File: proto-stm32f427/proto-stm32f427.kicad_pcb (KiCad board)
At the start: 2 copper layers, 54.6 x 66.7 mm, 37 parts, among them J1 Left, J2 Micro_SD_Card, J3 USB, J4 Debug, J5 Right, U1 NCV5501, U2 STM32F427VGTx, Y1 8 MHz

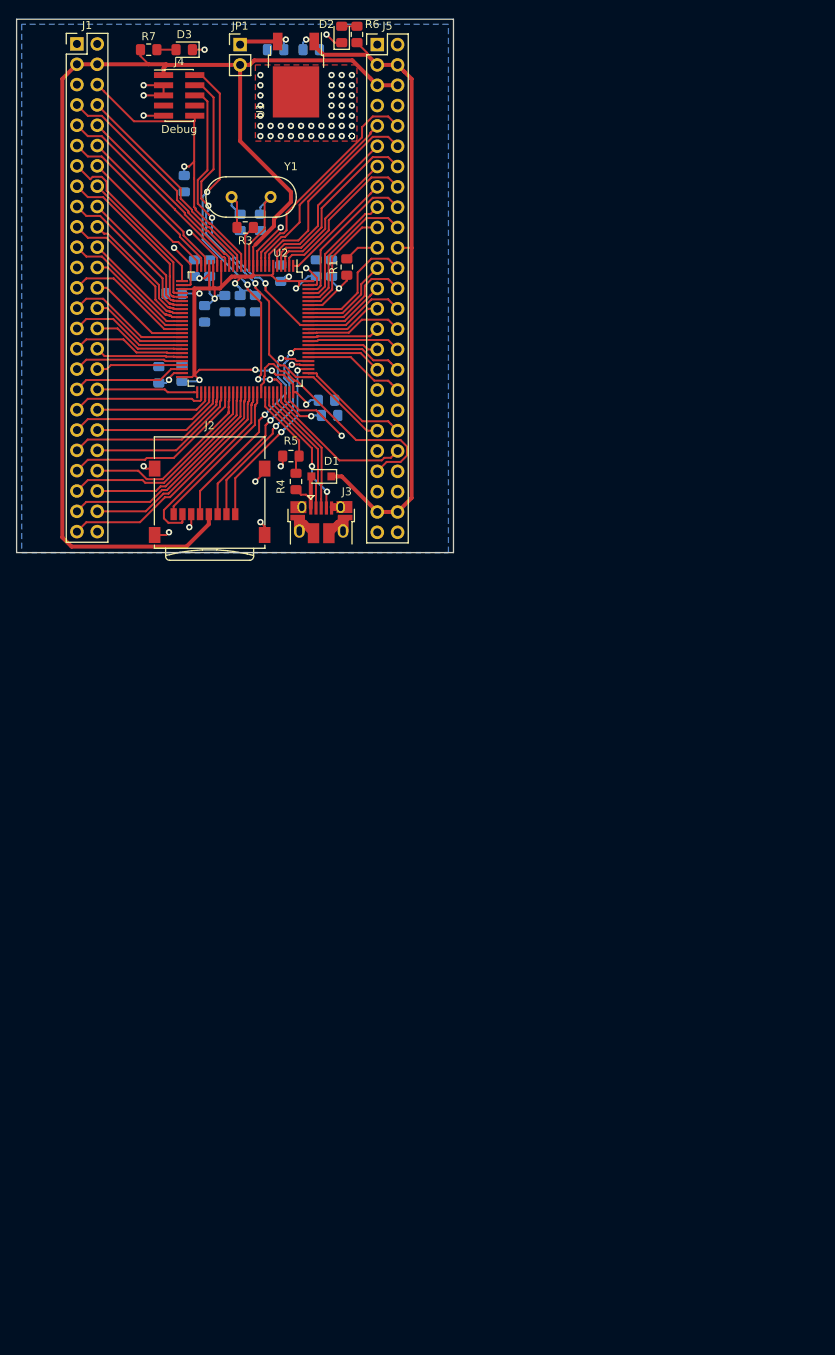
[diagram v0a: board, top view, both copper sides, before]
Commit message: New improved core board for stm32f427
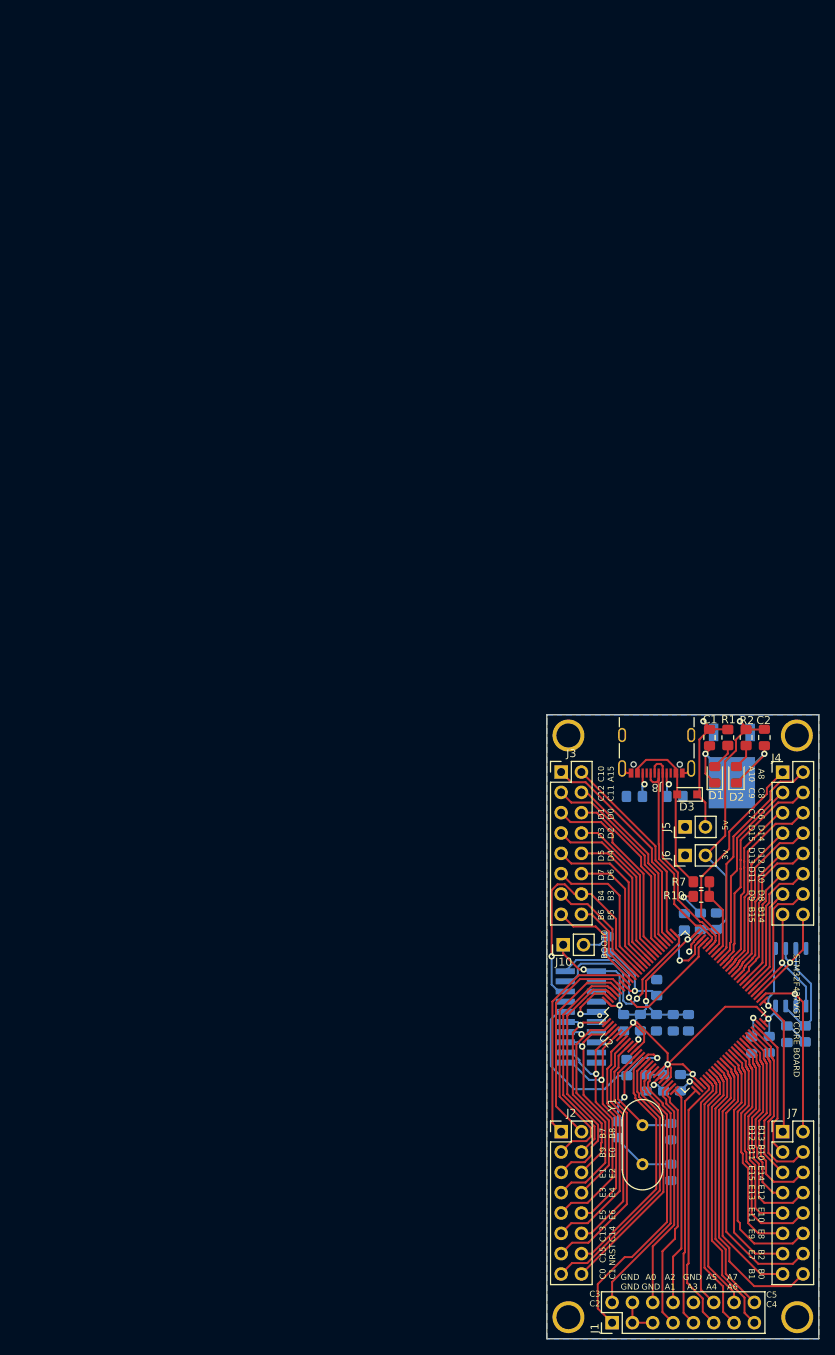
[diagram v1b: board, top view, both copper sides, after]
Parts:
- removed JP1: Idd, Connector_PinHeader_2.54mm:PinHeader_1x02_P2.54mm_Vertical
- added C19: 0.1 uF, Capacitor_SMD:C_0805_2012Metric_Pad1.18x1.45mm_HandSolder, B.Cu at (154.7, 147.8)
- added J10: BOOT, Connector_PinHeader_2.54mm:PinHeader_1x02_P2.54mm_Vertical, F.Cu at (126.7, 136.7)
- added J6: PWR_3v, Connector_PinHeader_2.54mm:PinHeader_1x02_P2.54mm_Vertical, F.Cu at (142.0, 125.5)
- added J7: Conn_02x08_Odd_Even, Connector_PinHeader_2.54mm:PinHeader_2x08_P2.54mm_Vertical, F.Cu at (154.2, 160.0)
- added J8: USB_C_Receptacle_USB2.0, Connector_USB:USB_C_Receptacle_GCT_USB4105-xx-A_16P_TopMnt_Horizontal, F.Cu at (138.4, 111.5)
- added J9: Conn_ARM_ETM_SWD_20, Connector_PinHeader_1.27mm:PinHeader_2x10_P1.27mm_Vertical_SMD, B.Cu at (128.9, 145.7)
- added R10: 10k, Resistor_SMD:R_0805_2012Metric_Pad1.20x1.40mm_HandSolder, F.Cu at (144.0, 130.6)
- added R8: 5.1k, Resistor_SMD:R_0805_2012Metric_Pad1.20x1.40mm_HandSolder, B.Cu at (140.7, 118.1)
- added R9: 10k, Resistor_SMD:R_0805_2012Metric_Pad1.20x1.40mm_HandSolder, B.Cu at (157.0, 147.8)
- added REF**: MountingHole_2.5mm_Pad, MountingHole:MountingHole_2.5mm_Pad, F.Cu at (156.0, 183.2)
- added REF**: MountingHole_2.5mm_Pad, MountingHole:MountingHole_2.5mm_Pad, F.Cu at (156.0, 110.5)
- added REF**: MountingHole_2.5mm_Pad, MountingHole:MountingHole_2.5mm_Pad, F.Cu at (127.4, 183.2)
- added REF**: MountingHole_2.5mm_Pad, MountingHole:MountingHole_2.5mm_Pad, F.Cu at (127.4, 110.5)
- added U3: W25Q32JVSS, Package_SO:SOIC-8_5.23x5.23mm_P1.27mm, B.Cu at (155.2, 140.7)
- C1, C2: moved to F.Cu
- C3, C5: value 16 pF -> 2.2 uF
- C4, C6: value 2.2 uF -> 16 pF
- D1: value BAT48JFILM -> LED; footprint Diode_SMD:D_SOD-323_HandSoldering -> LED_SMD:LED_0805_2012Metric_Pad1.15x1.40mm_HandSolder
- D3: value LED -> BAT48JFILM; footprint LED_SMD:LED_0805_2012Metric_Pad1.15x1.40mm_HandSolder -> Diode_SMD:D_SOD-323_HandSoldering
- J1: value Left -> Conn_02x08_Odd_Even; footprint Connector_PinHeader_2.54mm:PinHeader_2x25_P2.54mm_Vertical -> Connector_PinHeader_2.54mm:PinHeader_2x08_P2.54mm_Vertical
- J2: value Micro_SD_Card -> Conn_02x08_Odd_Even; footprint Connector_Card:microSD_HC_Wuerth_693072010801 -> Connector_PinHeader_2.54mm:PinHeader_2x08_P2.54mm_Vertical
- J3: value USB -> Conn_02x08_Odd_Even; footprint Connector_USB:USB_Micro-B_Amphenol_10103594-0001LF_Horizontal -> Connector_PinHeader_2.54mm:PinHeader_2x08_P2.54mm_Vertical
- J4: value Debug -> Conn_02x08_Odd_Even; footprint Connector_PinHeader_1.27mm:PinHeader_2x05_P1.27mm_Vertical_SMD -> Connector_PinHeader_2.54mm:PinHeader_2x08_P2.54mm_Vertical
- J5: value Right -> PWR_5v; footprint Connector_PinHeader_2.54mm:PinHeader_2x25_P2.54mm_Vertical -> Connector_PinHeader_2.54mm:PinHeader_1x02_P2.54mm_Vertical
- R1: value 1k -> 220; footprint Resistor_SMD:R_0805_2012Metric_Pad1.15x1.40mm_HandSolder -> Resistor_SMD:R_0805_2012Metric_Pad1.20x1.40mm_HandSolder
- R2: value 100k -> 220; footprint Resistor_SMD:R_0805_2012Metric_Pad1.15x1.40mm_HandSolder -> Resistor_SMD:R_0805_2012Metric_Pad1.20x1.40mm_HandSolder; moved to F.Cu
- R3: value 220 -> 1k; footprint Resistor_SMD:R_0805_2012Metric_Pad1.15x1.40mm_HandSolder -> Resistor_SMD:R_0805_2012Metric_Pad1.20x1.40mm_HandSolder; moved to B.Cu
- R4: value 4.7k -> 100k; footprint Resistor_SMD:R_0805_2012Metric_Pad1.15x1.40mm_HandSolder -> Resistor_SMD:R_0805_2012Metric_Pad1.20x1.40mm_HandSolder; moved to B.Cu
- R5: value 10k -> 220; footprint Resistor_SMD:R_0805_2012Metric_Pad1.15x1.40mm_HandSolder -> Resistor_SMD:R_0805_2012Metric_Pad1.20x1.40mm_HandSolder; moved to B.Cu
- R6: value 220 -> 5.1k; footprint Resistor_SMD:R_0805_2012Metric_Pad1.15x1.40mm_HandSolder -> Resistor_SMD:R_0805_2012Metric_Pad1.20x1.40mm_HandSolder; moved to B.Cu
- R7: value 220 -> 4.7k; footprint Resistor_SMD:R_0805_2012Metric_Pad1.15x1.40mm_HandSolder -> Resistor_SMD:R_0805_2012Metric_Pad1.20x1.40mm_HandSolder
- U1: moved to B.Cu
- moved J1 173.3 mm to (132.9, 183.9), turned to 90 degrees
- moved Y1 125.0 mm to (136.7, 159.2), turned to -90 degrees
- moved R7 124.9 mm to (144.0, 128.8), turned to 180 degrees
- moved C18 123.6 mm to (134.7, 152.0), turned to 90 degrees
- moved C17 120.8 mm to (152.5, 149.1), turned to 90 degrees
- moved C3 119.8 mm to (150.3, 149.2), turned to -90 degrees
- moved C7 115.5 mm to (137.1, 153.9), turned to -90 degrees
- moved C4 114.2 mm to (140.2, 160.0)
- moved J4 113.3 mm to (154.2, 115.1)
- moved C9 112.8 mm to (141.4, 153.9)
- moved D3 112.3 mm to (142.2, 117.9)
- moved C8 112.0 mm to (139.3, 153.9)
- moved C2 105.5 mm to (151.9, 110.7), turned to -90 degrees
- moved J5 105.1 mm to (142.0, 121.9), turned to 90 degrees
- moved C11 104.9 mm to (140.5, 146.4)
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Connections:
- C2 pad 1: /3v_regulated -> /3v_cpu
- C3 pad 1: GND -> Net-(C3-Pad1)
- C3 pad 2: /PH0 -> GND
- C4 pad 1: Net-(C4-Pad1) -> GND
- C4 pad 2: GND -> /PH0
- C5 pad 1: GND -> Net-(C5-Pad1)
- C5 pad 2: Net-(C5-Pad2) -> GND
- C6 pad 1: Net-(C6-Pad1) -> GND
- C6 pad 2: GND -> Net-(C6-Pad2)
- D1 pad 1: /5v -> GND
- D1 pad 2: /5v_usb -> Net-(D1-Pad2)
- D3 pad 1: GND -> /5v
- D3 pad 2: Net-(D3-Pad2) -> /5v_usb
- J1 pad 1: GND -> /PC2
- J1 pad 10: /PC2 -> GND
- J1 pad 11: /PA1 -> /PA4
- J1 pad 12: /PA0 -> /PA5
- J1 pad 13: /PA3 -> /PA6
- J1 pad 14: /PA2 -> /PA7
- J1 pad 15: /PA5 -> /PC4
- J1 pad 16: /PA4 -> /PC5
- J1 pad 2: GND -> /PC3
- J1 pad 3: /3v_cpu -> GND
- J1 pad 4: /3v_cpu -> GND
- J1 pad 6: /NRST -> /PA0
- J1 pad 7: /PC1 -> /PA1
- J1 pad 8: /PC0 -> /PA2
- J1 pad 9: /PC3 -> /PA3
- J2 pad 1: /PC10 -> /PB7
- J2 pad 2: /PC11 -> /PB8
- J2 pad 3: /PD2 -> /PB9
- J2 pad 4: /3v_cpu -> /PE0
- J2 pad 5: /PC12 -> /PE1
- J2 pad 6: GND -> /PE2
- J2 pad 7: /PC8 -> /PE3
- J2 pad 8: /PC9 -> /PE4
- J2 pad 9: GND -> /PE5
- J3 pad 1: /5v_usb -> /PC10
- J3 pad 2: /PA11 -> /PA15
- J3 pad 3: /PA12 -> /PC12
- J3 pad 4: /PA10 -> /PC11
- J3 pad 5: GND -> /PD1
- J3 pad 6: GND -> /PD0
- J4 pad 1: /3v_cpu -> /PA10
- J4 pad 10: /NRST -> /PD12
- J4 pad 2: /PA13 -> /PA8
- J4 pad 3: GND -> /PC9
- J4 pad 4: /PA14 -> /PC8
- J4 pad 5: GND -> /PC7
- J4 pad 6: /PB3 -> /PC6
- J4 pad 7: Net-(J4-Pad7) -> /PD15
- J4 pad 8: Net-(J4-Pad8) -> /PD14
- J4 pad 9: GND -> /PD13
- J5 pad 2: GND -> /5v
- R1 pad 1: Net-(R1-Pad1) -> /5v
- R1 pad 2: /BOOT0 -> Net-(D1-Pad2)
- R2 pad 1: GND -> /3v_cpu
- R2 pad 2: Net-(R1-Pad1) -> Net-(D2-Pad2)
- R3 pad 1: /PH1 -> Net-(R3-Pad1)
- R3 pad 2: Net-(C5-Pad2) -> /BOOT0
- R4 pad 1: /PA9 -> GND
- R4 pad 2: /5v_usb -> Net-(R3-Pad1)
- R5 pad 1: /PA9 -> /PH1
- R5 pad 2: GND -> Net-(C6-Pad2)
- R6 pad 1: /5v -> /CC2
- R6 pad 2: Net-(D2-Pad2) -> GND
- R7 pad 1: /3v_cpu -> /PA9
- R7 pad 2: Net-(D3-Pad2) -> /5v_usb
- U1 pad 3: /3v_regulated -> /3v_cpu
- U2 pad 49: Net-(C4-Pad1) -> Net-(C3-Pad1)
- U2 pad 73: Net-(C6-Pad1) -> Net-(C5-Pad1)
- U2 pad 94: Net-(R1-Pad1) -> Net-(R3-Pad1)
- Y1 pad 2: Net-(C5-Pad2) -> Net-(C6-Pad2)
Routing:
- net /3v_cpu: track 246.0 -> 138.5 mm, vias 10 -> 9
- net /5v: track 85.7 -> 18.8 mm
- net /PA13: track 67.4 -> 26.3 mm, vias 4 -> 1
- net /PA14: track 57.0 -> 25.5 mm, vias 2 -> 1
- net /PB0: track 14.2 -> 37.3 mm
- net /PB2: track 13.6 -> 34.5 mm
- net /PE8: track 12.4 -> 32.2 mm
- net /PD2: track 39.1 -> 20.0 mm, vias 2 -> 0
- net /NRST: track 38.0 -> 57.0 mm
- net /PC4: track 15.8 -> 34.7 mm
- net /PB3: track 50.0 -> 31.5 mm, vias 2 -> 1
- net /PE10: track 12.3 -> 29.6 mm
- net /PA6: track 16.9 -> 33.3 mm
- net /PE12: track 11.7 -> 27.2 mm
- net /PB1: track 17.0 -> 32.3 mm
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- removed copper zone on F.Cu, net GND
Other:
- board size 54.6 x 66.7 mm -> 34 x 78 mm
- net class Default removed
- board text added: "A0 GND"
- board text added: "A2 A1"
- board text added: "A5 A4"
- board text added: "A7 A6"
- board text added: "A8 A10"
- board text added: "B0 B1"
- board text added: "B10 B11"
- board text added: "B13 B12"
- board text added: "B14 B15"
- board text added: "B2 E7"
- board text added: "B4 B3"
- board text added: "B6 B5"
- board text added: "B7 B8"
- board text added: "B9 E0"
- board text added: "C0 C1"
- board text added: "C10 A15"
- board text added: "C12 C11"
- board text added: "C13 C14"
- board text added: "C15 NRST"
- board text added: "C3 C2"
- board text added: "C5 C4"
- board text added: "C6 C7"
- board text added: "C8 C9"
- board text added: "D1 D0"
- board text added: "D10 D11"
- board text added: "D12 D13"
- board text added: "D14 D15"
- board text added: "D3 D2"
- board text added: "D5 D4"
- board text added: "D7 D6"
- board text added: "D8 D9"
- board text added: "E1 E2"
- board text added: "E10 E11"
- board text added: "E12 E13"
- board text added: "E14 E15"
- board text added: "E3 E4"
- board text added: "E5 E6"
- board text added: "E8 E9"
- board text added: "ETM TRACE"
- board text added: "GND A3"
- board text added: "GND GND"
- board text added: "SPI1 FLASH"
- board text added: "STM32F427VGT CORE BOARD"
- board text removed: "A0"
- board text removed: "A1"
- board text removed: "A13"
- board text removed: "A14"
- board text removed: "A15"
- board text removed: "A2"
- board text removed: "A3"
- board text removed: "A4"
- board text removed: "A5"
- board text removed: "A6"
- board text removed: "A7"
- board text removed: "A8"
- board text removed: "B0"
- board text removed: "B1"
- board text removed: "B10"
- board text removed: "B11"
- board text removed: "B12"
- board text removed: "B13"
- board text removed: "B14"
- board text removed: "B15"
- board text removed: "B2"
- board text removed: "B3"
- board text removed: "B4"
- board text removed: "B5"
- board text removed: "B6"
- board text removed: "B7"
- board text removed: "B8"
- board text removed: "B9"
- board text removed: "C0"
- board text removed: "C1"
- board text removed: "C13"
- board text removed: "C14"
- board text removed: "C15"
- board text removed: "C2"
- board text removed: "C3"
- board text removed: "C4"
- board text removed: "C5"
- board text removed: "C6"
- board text removed: "C7"
- board text removed: "D0"
- board text removed: "D1"
- board text removed: "D10"
- board text removed: "D11"
- board text removed: "D12"
- board text removed: "D13"
- board text removed: "D14"
- board text removed: "D15"
- board text removed: "D2"
- board text removed: "D3"
- board text removed: "D4"
- board text removed: "D5"
- board text removed: "D6"
- board text removed: "D7"
- board text removed: "D8"
- board text removed: "D9"
- board text removed: "E0"
- board text removed: "E1"
- board text removed: "E10"
- board text removed: "E11"
- board text removed: "E12"
- board text removed: "E13"
- board text removed: "E14"
- board text removed: "E15"
- board text removed: "E2"
- board text removed: "E3"
- board text removed: "E4"
- board text removed: "E5"
- board text removed: "E6"
- board text removed: "E7"
- board text removed: "E8"
- board text removed: "E9"
- board text removed: "GND"
- board text removed: "RST"

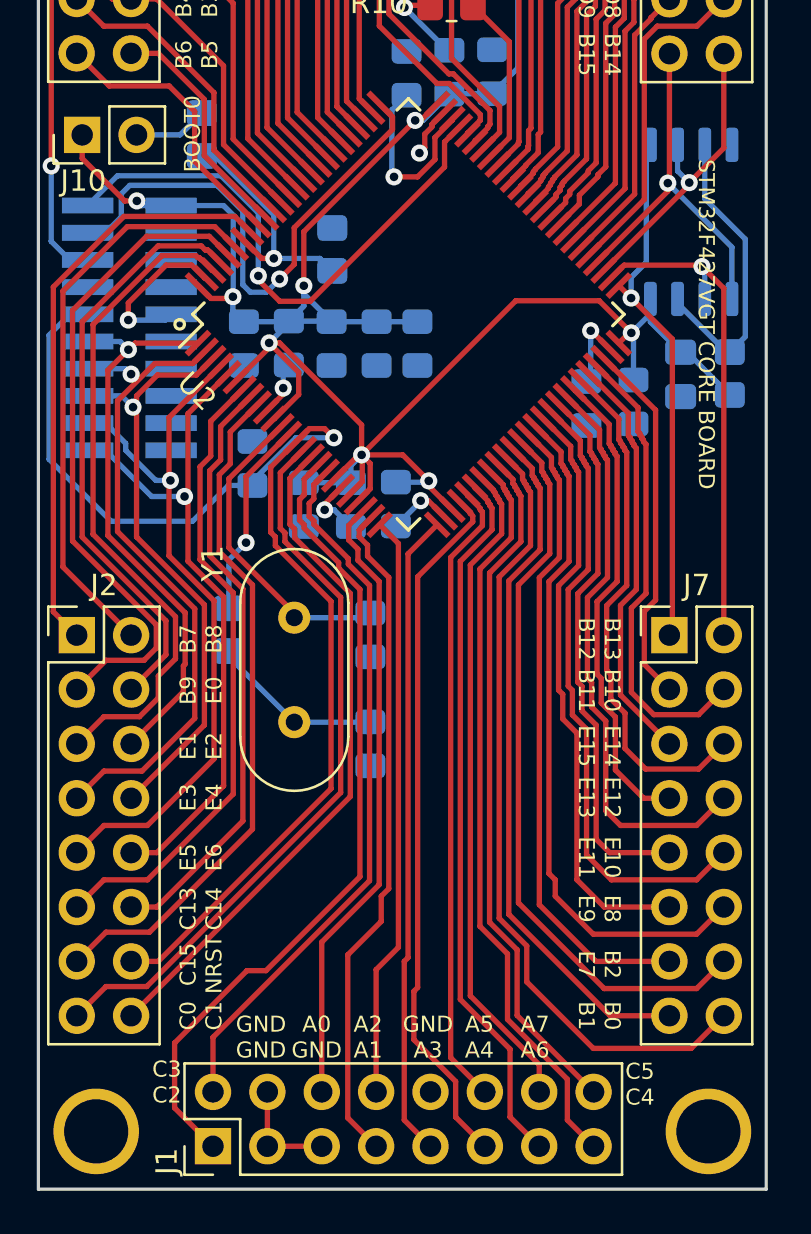
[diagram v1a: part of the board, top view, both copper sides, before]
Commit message: Change out footprint for stm32h7 and rewire pins to accomodate
Same basic board, but now should mostly support the F7 and H7 series
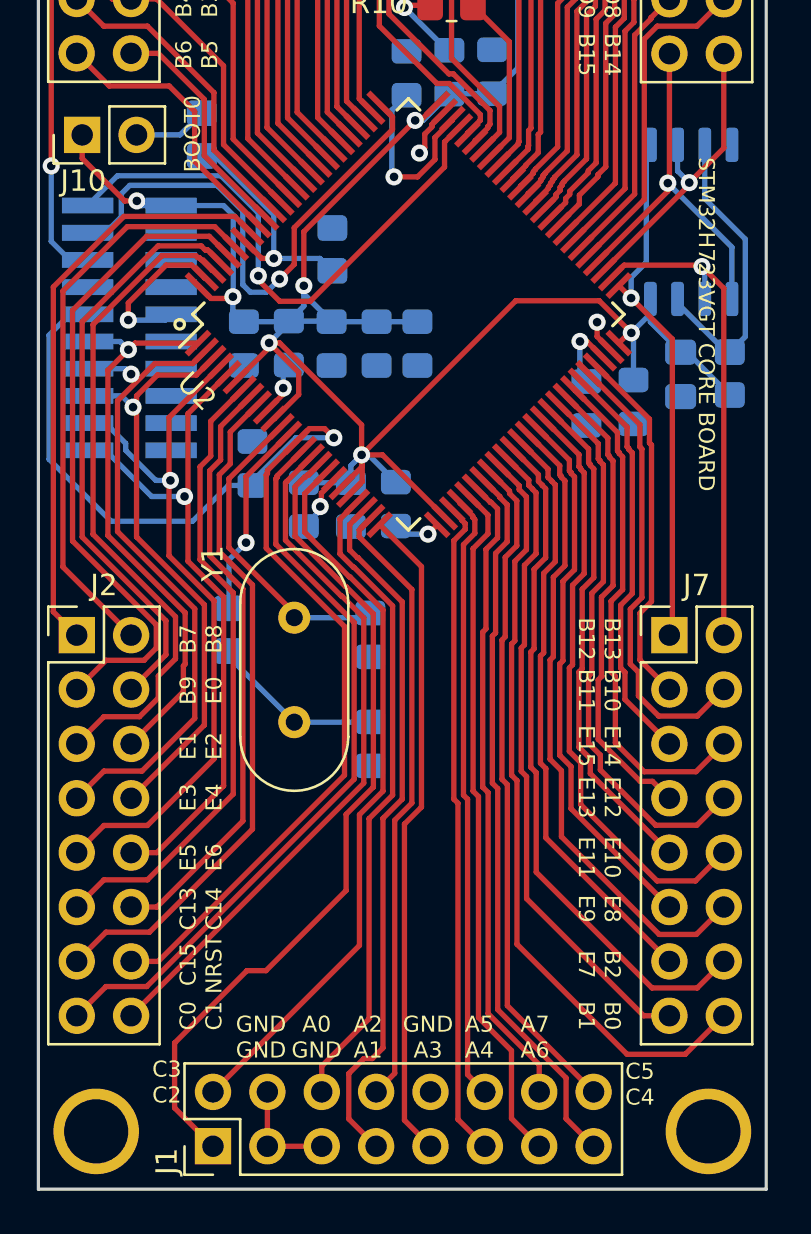
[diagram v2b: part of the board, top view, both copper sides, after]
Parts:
- U2: value STM32F427VGTx -> STM32H743VITx
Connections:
- U2 pad 19: /3v_cpu -> GND
- U2 pad 20: GND -> /3v_cpu
- U2 pad 22: /3v_cpu -> /PA0
- U2 pad 23: /PA0 -> /PA1
- U2 pad 24: /PA1 -> /PA2
- U2 pad 25: /PA2 -> /PA3
- U2 pad 26: /PA3 -> GND
- U2 pad 27: GND -> /3v_cpu
- U2 pad 28: /3v_cpu -> /PA4
- U2 pad 29: /PA4 -> /PA5
- U2 pad 30: /PA5 -> /PA6
- U2 pad 31: /PA6 -> /PA7
- U2 pad 32: /PA7 -> /PC4
- U2 pad 33: /PC4 -> /PC5
- U2 pad 34: /PC5 -> /PB0
- U2 pad 35: /PB0 -> /PB1
- U2 pad 36: /PB1 -> /PB2
- U2 pad 37: /PB2 -> /PE7
- U2 pad 38: /PE7 -> /PE8
- U2 pad 39: /PE8 -> /PE9
- U2 pad 40: /PE9 -> /PE10
- U2 pad 41: /PE10 -> /PE11
- U2 pad 42: /PE11 -> /PE12
- U2 pad 43: /PE12 -> /PE13
- U2 pad 44: /PE13 -> /PE14
- U2 pad 45: /PE14 -> /PE15
- U2 pad 46: /PE15 -> /PB10
- U2 pad 47: /PB10 -> /PB11
- U2 pad 48: /PB11 -> Net-(C3-Pad1)
- U2 pad 49: Net-(C3-Pad1) -> GND
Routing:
- net /PE7: track 30.2 -> 27.7 mm
- net /3v_cpu: track 138.5 -> 136.3 mm, vias 9 -> 8
- net /PE8: track 32.2 -> 30.0 mm
- net /PB2: track 34.5 -> 32.3 mm
- net /PE9: track 27.8 -> 25.6 mm
- net /PA4: track 32.9 -> 30.8 mm
- net /PE11: track 25.5 -> 23.5 mm
- net /PB1: track 32.3 -> 30.6 mm
- net /PE10: track 29.6 -> 28.0 mm
- net /PA2: track 27.3 -> 28.8 mm
- net /PE12: track 27.2 -> 25.9 mm
- net /PB0: track 37.3 -> 35.9 mm
- net /PA1: track 31.6 -> 32.9 mm
- net /PA0: track 29.2 -> 30.3 mm
- net /PA5: track 29.5 -> 28.5 mm
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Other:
- board text added: "STM32H723VGT CORE BOARD"
- board text removed: "STM32F427VGT CORE BOARD"
